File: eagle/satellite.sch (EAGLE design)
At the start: 10 parts

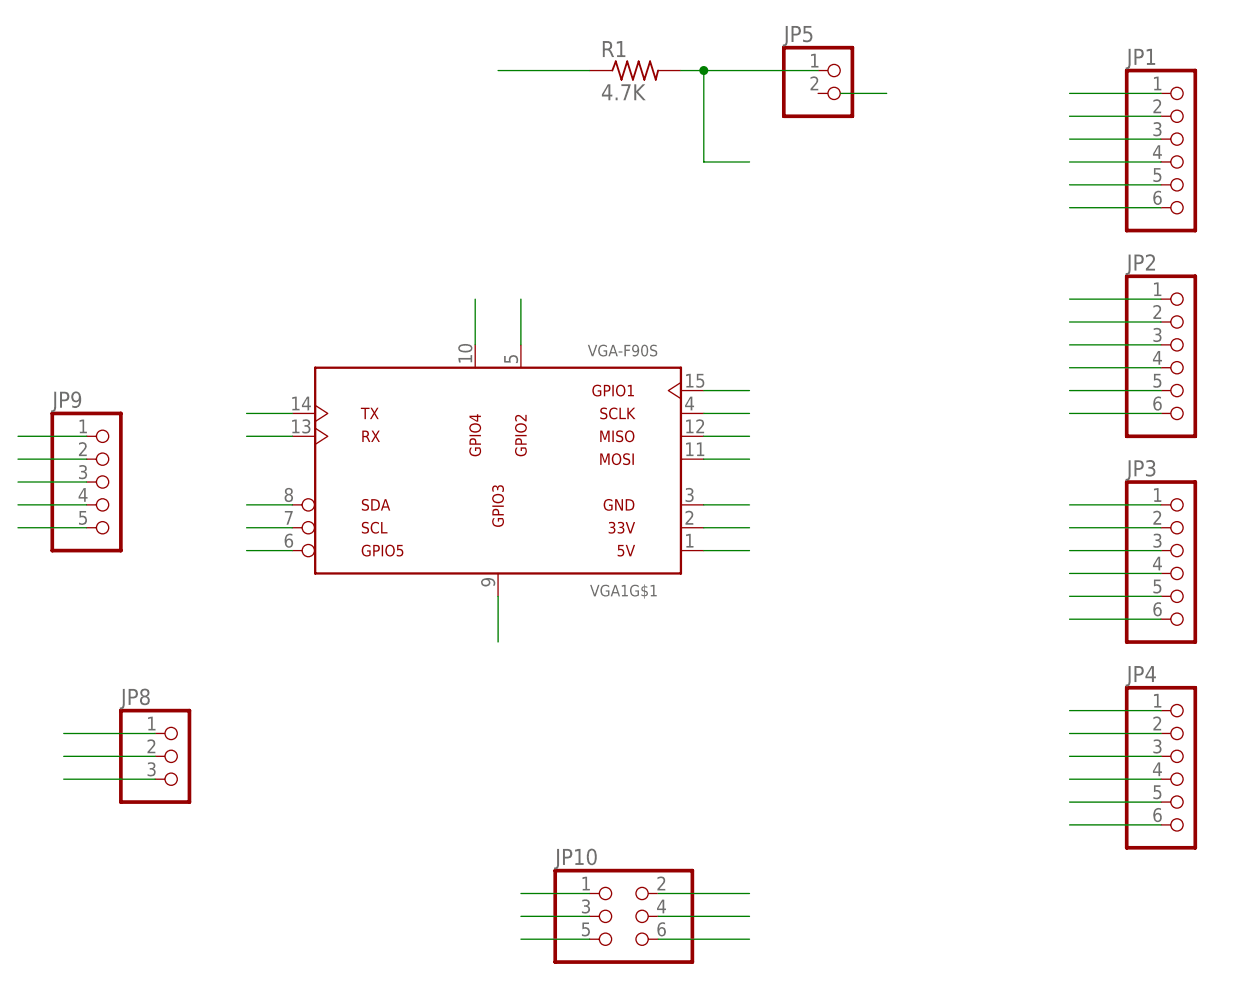
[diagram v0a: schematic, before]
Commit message: eagle file changes that were submitted for a quote
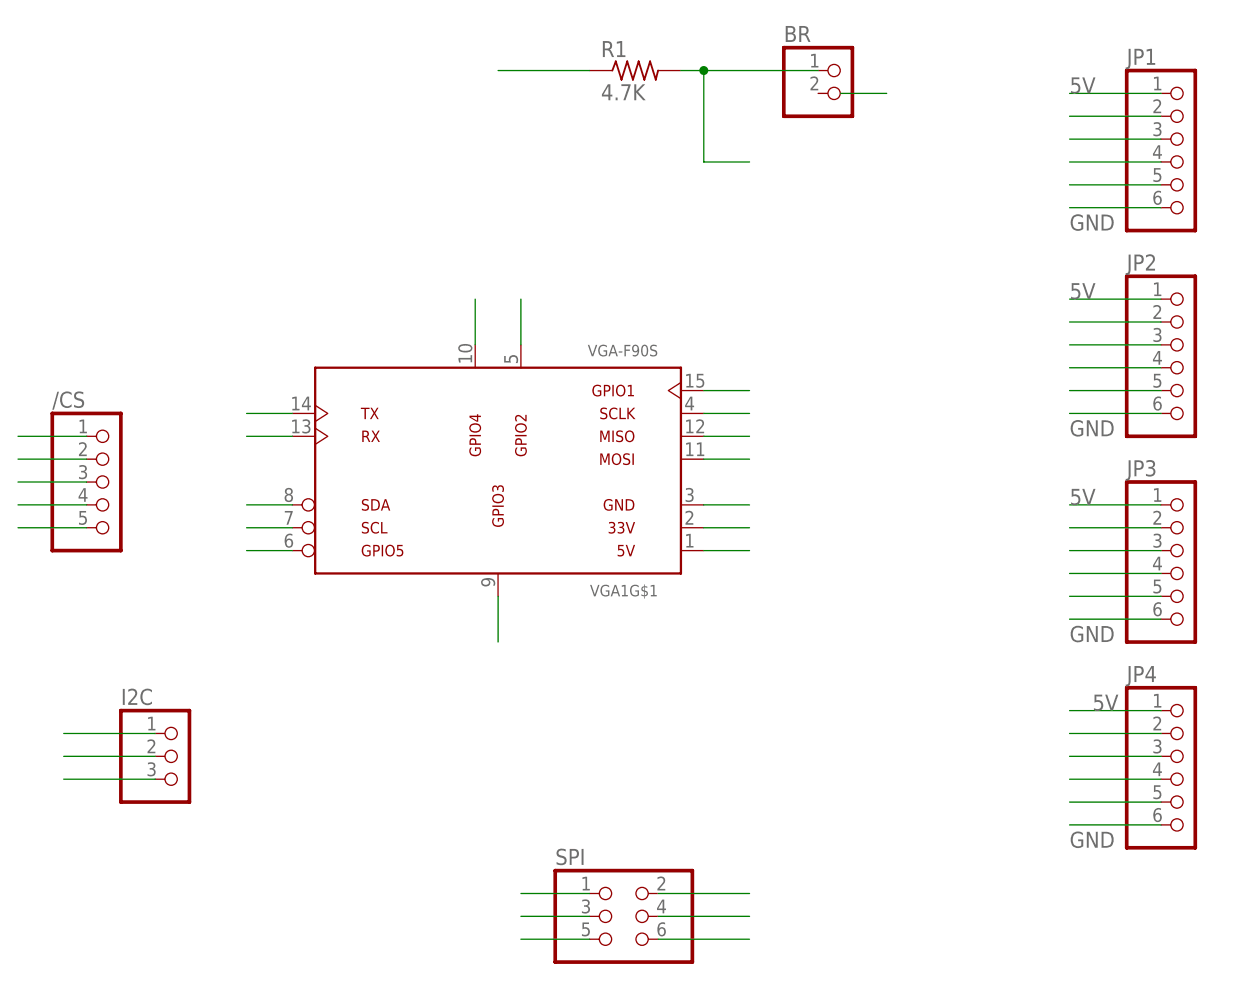
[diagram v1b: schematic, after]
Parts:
- renumbered JP10 to SPI, JP5 to BR, JP8 to I2C, JP9 to /CS
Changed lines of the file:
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@@
 <part name="JP4" library="pinhead" deviceset="PINHD-1X6" device=""/>
 <part name="R1" library="rcl" deviceset="R-US_" device="0204/5" value="4.7K"/>
-<part name="JP5" library="pinhead" deviceset="PINHD-1X2" device=""/>
-<part name="JP8" library="pinhead" deviceset="PINHD-1X3" device=""/>
-<part name="JP9" library="pinhead" deviceset="PINHD-1X5" device=""/>
-<part name="JP10" library="pinhead" deviceset="PINHD-2X3" device=""/>
+<part name="BR" library="pinhead" deviceset="PINHD-1X2" device=""/>
+<part name="I2C" library="pinhead" deviceset="PINHD-1X3" device=""/>
+<part name="/CS" library="pinhead" deviceset="PINHD-1X5" device=""/>
+<part name="SPI" library="pinhead" deviceset="PINHD-2X3" device=""/>
 </parts>
 <sheets>
@@
 <instance part="JP4" gate="A" x="149.86" y="27.94"/>
 <instance part="R1" gate="G$1" x="88.9" y="106.68"/>
-<instance part="JP5" gate="G$1" x="111.76" y="104.14"/>
-<instance part="JP8" gate="A" x="38.1" y="30.48"/>
-<instance part="JP9" gate="A" x="30.48" y="60.96"/>
-<instance part="JP10" gate="A" x="86.36" y="12.7"/>
+<instance part="BR" gate="G$1" x="111.76" y="104.14"/>
+<instance part="I2C" gate="A" x="38.1" y="30.48"/>
+<instance part="/CS" gate="A" x="30.48" y="60.96"/>
+<instance part="SPI" gate="A" x="86.36" y="12.7"/>
 </instances>
 <busses>
@@
 </segment>
 <segment>
-<pinref part="JP10" gate="A" pin="3"/>
+<pinref part="SPI" gate="A" pin="3"/>
 <wire x1="76.2" y1="12.7" x2="83.82" y2="12.7" width="0.1524" layer="91"/>
 </segment>
@@
 <segment>
 <pinref part="R1" gate="G$1" pin="2"/>
-<pinref part="JP5" gate="G$1" pin="1"/>
+<pinref part="BR" gate="G$1" pin="1"/>
 <wire x1="93.98" y1="106.68" x2="96.52" y2="106.68" width="0.1524" layer="91"/>
 <wire x1="96.52" y1="106.68" x2="109.22" y2="106.68" width="0.1524" layer="91"/>
@@
 <pinref part="JP1" gate="A" pin="1"/>
 <wire x1="147.32" y1="104.14" x2="137.16" y2="104.14" width="0.1524" layer="91"/>
+<label x="137.16" y="104.14" size="1.778" layer="95"/>
 </segment>
 <segment>
 <pinref part="JP2" gate="A" pin="1"/>
 <wire x1="147.32" y1="81.28" x2="137.16" y2="81.28" width="0.1524" layer="91"/>
+<label x="137.16" y="81.28" size="1.778" layer="95"/>
 </segment>
 <segment>
 <pinref part="JP3" gate="A" pin="1"/>
 <wire x1="147.32" y1="58.42" x2="137.16" y2="58.42" width="0.1524" layer="91"/>
+<label x="137.16" y="58.42" size="1.778" layer="95"/>
 </segment>
 <segment>
 <pinref part="JP4" gate="A" pin="1"/>
 <wire x1="147.32" y1="35.56" x2="137.16" y2="35.56" width="0.1524" layer="91"/>
+<label x="139.7" y="35.56" size="1.778" layer="95"/>
 </segment>
 <segment>
@@
 </segment>
 <segment>
-<pinref part="JP10" gate="A" pin="2"/>
+<pinref part="SPI" gate="A" pin="2"/>
 <wire x1="101.6" y1="15.24" x2="91.44" y2="15.24" width="0.1524" layer="91"/>
 </segment>
@@
 </segment>
 <segment>
-<pinref part="JP10" gate="A" pin="1"/>
+<pinref part="SPI" gate="A" pin="1"/>
 <wire x1="83.82" y1="15.24" x2="76.2" y2="15.24" width="0.1524" layer="91"/>
 </segment>
@@
 </segment>
 <segment>
-<pinref part="JP8" gate="A" pin="1"/>
+<pinref part="I2C" gate="A" pin="1"/>
 <wire x1="35.56" y1="33.02" x2="25.4" y2="33.02" width="0.1524" layer="91"/>
 </segment>
@@
 </segment>
 <segment>
-<pinref part="JP8" gate="A" pin="2"/>
+<pinref part="I2C" gate="A" pin="2"/>
 <wire x1="35.56" y1="30.48" x2="25.4" y2="30.48" width="0.1524" layer="91"/>
 </segment>
@@
 </segment>
 <segment>
-<pinref part="JP9" gate="A" pin="5"/>
+<pinref part="/CS" gate="A" pin="5"/>
 <wire x1="20.32" y1="55.88" x2="27.94" y2="55.88" width="0.1524" layer="91"/>
 </segment>
@@
 </segment>
 <segment>
-<pinref part="JP9" gate="A" pin="2"/>
+<pinref part="/CS" gate="A" pin="2"/>
 <wire x1="20.32" y1="63.5" x2="27.94" y2="63.5" width="0.1524" layer="91"/>
 </segment>
@@
 </segment>
 <segment>
-<pinref part="JP9" gate="A" pin="3"/>
+<pinref part="/CS" gate="A" pin="3"/>
 <wire x1="20.32" y1="60.96" x2="27.94" y2="60.96" width="0.1524" layer="91"/>
 </segment>
@@
 </segment>
 <segment>
-<pinref part="JP9" gate="A" pin="1"/>
+<pinref part="/CS" gate="A" pin="1"/>
 <wire x1="20.32" y1="66.04" x2="27.94" y2="66.04" width="0.1524" layer="91"/>
 </segment>
@@
 </segment>
 <segment>
-<pinref part="JP9" gate="A" pin="4"/>
+<pinref part="/CS" gate="A" pin="4"/>
 <wire x1="20.32" y1="58.42" x2="27.94" y2="58.42" width="0.1524" layer="91"/>
 </segment>
@@
 </segment>
 <segment>
-<pinref part="JP10" gate="A" pin="4"/>
+<pinref part="SPI" gate="A" pin="4"/>
 <wire x1="91.44" y1="12.7" x2="101.6" y2="12.7" width="0.1524" layer="91"/>
 </segment>
@@
 <pinref part="JP1" gate="A" pin="6"/>
 <wire x1="137.16" y1="91.44" x2="147.32" y2="91.44" width="0.1524" layer="91"/>
+<label x="137.16" y="88.9" size="1.778" layer="95"/>
 </segment>
 <segment>
 <pinref part="JP2" gate="A" pin="6"/>
 <wire x1="147.32" y1="68.58" x2="137.16" y2="68.58" width="0.1524" layer="91"/>
+<label x="137.16" y="66.04" size="1.778" layer="95"/>
 </segment>
 <segment>
 <pinref part="JP3" gate="A" pin="6"/>
 <wire x1="147.32" y1="45.72" x2="137.16" y2="45.72" width="0.1524" layer="91"/>
+<label x="137.16" y="43.18" size="1.778" layer="95"/>
 </segment>
 <segment>
 <pinref part="JP4" gate="A" pin="6"/>
 <wire x1="137.16" y1="22.86" x2="147.32" y2="22.86" width="0.1524" layer="91"/>
+<label x="137.16" y="20.32" size="1.778" layer="95"/>
 </segment>
 <segment>
@@
 </segment>
 <segment>
-<pinref part="JP10" gate="A" pin="6"/>
+<pinref part="SPI" gate="A" pin="6"/>
 <wire x1="101.6" y1="10.16" x2="91.44" y2="10.16" width="0.1524" layer="91"/>
 </segment>
 <segment>
-<pinref part="JP8" gate="A" pin="3"/>
+<pinref part="I2C" gate="A" pin="3"/>
 <wire x1="35.56" y1="27.94" x2="25.4" y2="27.94" width="0.1524" layer="91"/>
 </segment>
@@
 </segment>
 <segment>
-<pinref part="JP10" gate="A" pin="5"/>
+<pinref part="SPI" gate="A" pin="5"/>
 <wire x1="76.2" y1="10.16" x2="83.82" y2="10.16" width="0.1524" layer="91"/>
 </segment>

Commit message: wrote a bunch and added references and pictures
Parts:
- renumbered JP1 to PRESS1, JP2 to PRESS2, JP3 to PRESS3, JP4 to PRESS4
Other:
- moved on the sheet: /CS, BR, I2C, R1, SPI, VGA1G$1
